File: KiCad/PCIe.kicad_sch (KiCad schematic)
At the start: 2 parts

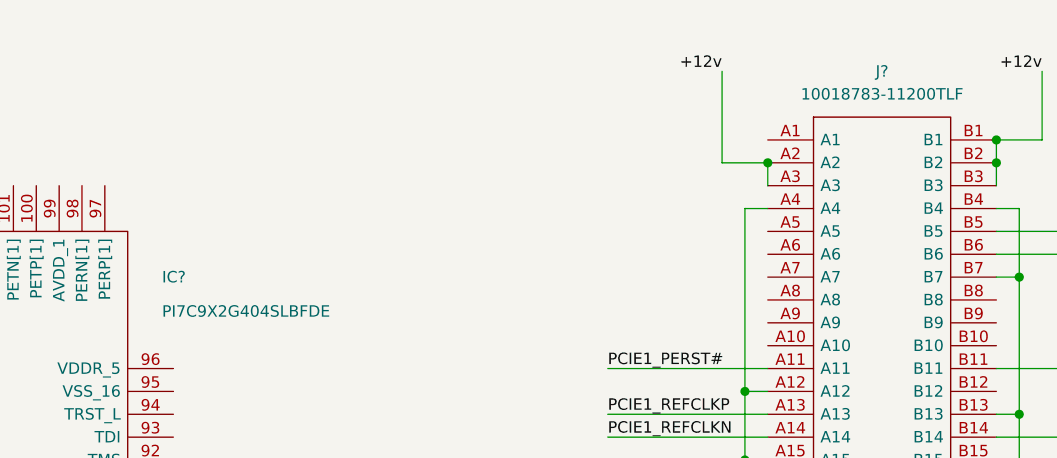
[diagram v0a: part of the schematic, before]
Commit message: Big changes (see expanded comment)
Added new components:
USB2517-JZX USB2.0 Hub
SI-52100-002 Vertical USB2.0 A Header

Began work on USB schematic, mostly done. Needs power delivery work done
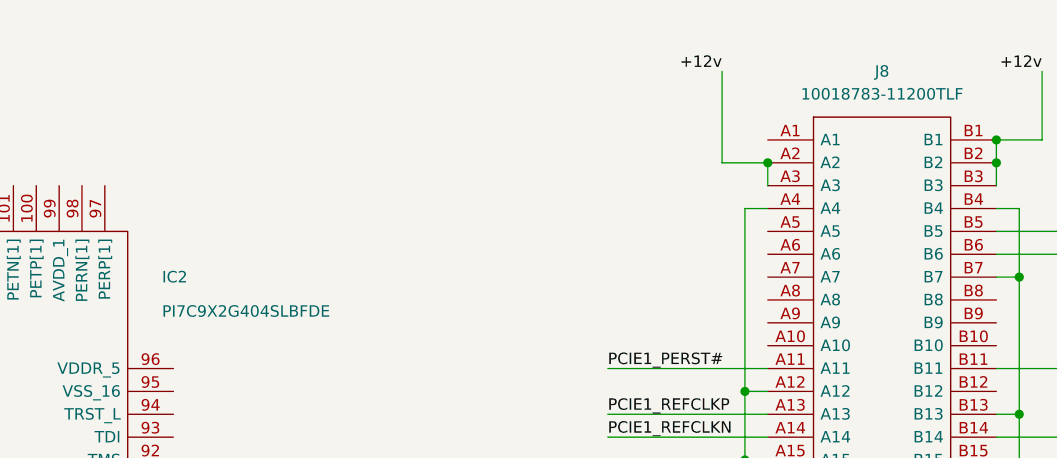
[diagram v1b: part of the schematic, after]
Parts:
- gave numbers to parts that had none: 2
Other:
- company: (none) -> TheGuyDanish
- title: (none) -> PCI-e Switch and Ports
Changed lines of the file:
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@@
 (kicad_sch (version 20200828) (generator eeschema)
-  (page 3 4)
+  (page 4 5)
   (paper "A4")
+  (title_block
+    (title "PCI-e Switch and Ports")
+    (date "2020-11-14")
+    (rev "0.1")
+    (company "TheGuyDanish")
+    (comment 1 "https://github.com/theguydanish/cm4_matx")
+  )
   (junction (at 190.5 58.42) (diameter 1.016) (color 0 0 0 0))
   (junction (at 190.5 66.04) (diameter 1.016) (color 0 0 0 0))
@@
   (symbol (lib_id "power:GND") (at 190.5 81.28 0) (unit 1)
     (in_bom yes) (on_board yes)
-    (property "Reference" "#PWR?" (id 0) (at 190.5 87.63 0)
+    (property "Reference" "#PWR0121" (id 0) (at 190.5 87.63 0)
       (effects (font (size 1.27 1.27)) hide)
     )
@@
   (symbol (lib_id "power:GND") (at 220.98 81.28 0) (unit 1)
     (in_bom yes) (on_board yes)
-    (property "Reference" "#PWR?" (id 0) (at 220.98 87.63 0)
+    (property "Reference" "#PWR0122" (id 0) (at 220.98 87.63 0)
       (effects (font (size 1.27 1.27)) hide)
     )
@@
   (symbol (lib_id "CM4_MATX:10018783-11200TLF") (at 193.04 30.48 0) (unit 1)
     (in_bom yes) (on_board yes)
-    (property "Reference" "J?" (id 0) (at 205.74 22.86 0))
+    (property "Reference" "J8" (id 0) (at 205.74 22.86 0))
     (property "Value" "10018783-11200TLF" (id 1) (at 205.74 25.4 0))
     (property "Footprint" "1001878410200TLF" (id 2) (at 214.63 27.94 0)
@@
   (symbol (lib_id "CM4_MATX:PI7C9X2G404SLBFDE") (at 30.48 55.88 0) (unit 1)
     (in_bom yes) (on_board yes)
-    (property "Reference" "IC?" (id 0) (at 125.73 45.72 0)
+    (property "Reference" "IC2" (id 0) (at 125.73 45.72 0)
       (effects (font (size 1.27 1.27)) (justify left))
     )
